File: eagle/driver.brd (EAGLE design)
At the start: 101.6 x 76.2 mm, 100 parts, among them IC1 XMEGA128A1, IC10 ST95P08M, IC11 ST95P08M, IC12 ST95P08M, IC13 ST95P08M, IC14 ST95P08M, IC15 ST95P08M, IC16 74AHC1G02DBV, IC17 74AHC1G02DBV, IC18 74AHC1G125DBV, IC19 74AHC1G125DBV, IC2 74AC16244, IC20 ST95P08M, IC21 ST95P08M, IC22 ST95P08M, IC23 ST95P08M, IC24 ST95P08M, IC25 ST95P08M, IC3 74AC16244, IC4 74AC16244, IC5 74AC16244, IC6 74AC16374, IC7 74AC16374, IC8 74AC16374, IC9 74AC16374, SW1 FSM2JSMA

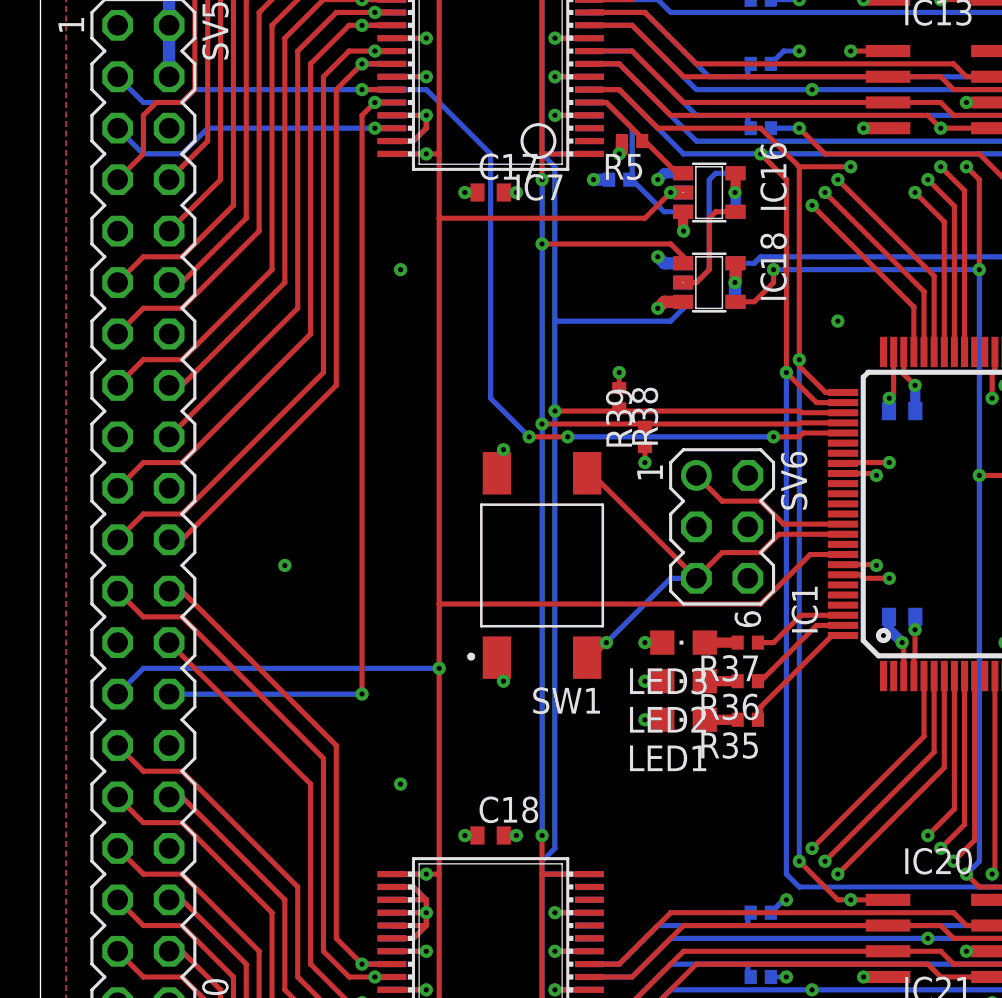
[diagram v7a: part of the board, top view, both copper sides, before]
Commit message: additional pull-up resistors
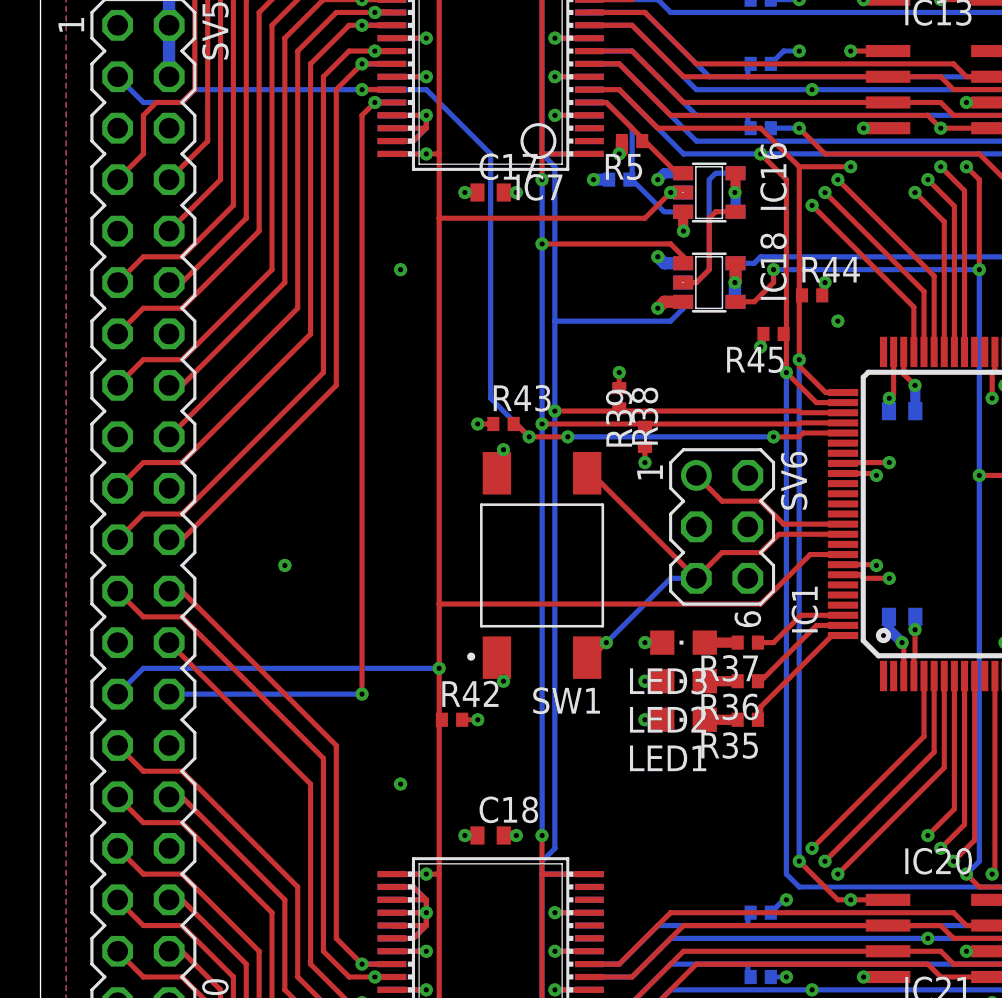
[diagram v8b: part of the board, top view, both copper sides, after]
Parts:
- added R42, R43, R44, R45: 33k, rcl:R0402
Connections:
- removed net N$92: IC6.27, IC7.46, SV5.5
- removed net N$99: IC1.92, IC16.2, IC17.2, IC6.25, IC6.48, IC7.25, IC7.48, IC8.25, IC8.48, IC9.25, IC9.48, SV5.27
- new net CLKIN: IC1.92, IC16.2, IC17.2, IC6.25, IC6.48, IC7.25, IC7.48, IC8.25, IC8.48, IC9.25, IC9.48, R42.1, SV5.27
- net GND: now also IC6.27, IC7.46, R42.2
- net VCC: now also R43.1, R44.2, R45.2
- net VSYNC: now also R43.2
- net VSYNC0: now also R45.1
- net VSYNC1: now also R44.1
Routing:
- net CLKIN: track 0.00 -> 130.9 mm, vias 0 -> 6
- net N$99: track 130.7 -> 0.00 mm, vias 6 -> 0
- net N$92: track 15.4 -> 0.00 mm, vias 1 -> 0
- net GND: track 194.6 -> 198.8 mm, vias 102 -> 103
- net VCC: track 86.1 -> 88.3 mm, vias 36 -> 39
- net VSYNC: track 52.3 -> 53.4 mm
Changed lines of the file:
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@@
 <attribute name="VALUE" x="70.485" y="39.37" size="1.27" layer="27" rot="R270"/>
+</element>
+<element name="R42" library="rcl" library_urn="urn:adsk.eagle:library:334" package="R0402" package3d_urn="urn:adsk.eagle:package:23547/3" value="33k" x="20.32" y="27.94" smashed="yes">
+<attribute name="NAME" x="19.685" y="28.575" size="1.27" layer="25"/>
+<attribute name="POPULARITY" value="34" x="20.32" y="27.94" size="1.778" layer="27" display="off"/>
+<attribute name="SPICEPREFIX" value="R" x="20.32" y="27.94" size="1.778" layer="27" display="off"/>
+<attribute name="VALUE" x="19.685" y="26.035" size="1.27" layer="27"/>
+</element>
+<element name="R43" library="rcl" library_urn="urn:adsk.eagle:library:334" package="R0402" package3d_urn="urn:adsk.eagle:package:23547/3" value="33k" x="22.86" y="42.545" smashed="yes">
+<attribute name="NAME" x="22.225" y="43.18" size="1.27" layer="25"/>
+<attribute name="POPULARITY" value="34" x="22.86" y="42.545" size="1.778" layer="27" display="off"/>
+<attribute name="SPICEPREFIX" value="R" x="22.86" y="42.545" size="1.778" layer="27" display="off"/>
+<attribute name="VALUE" x="22.225" y="40.64" size="1.27" layer="27"/>
+</element>
+<element name="R44" library="rcl" library_urn="urn:adsk.eagle:library:334" package="R0402" package3d_urn="urn:adsk.eagle:package:23547/3" value="33k" x="38.1" y="48.895" smashed="yes">
+<attribute name="NAME" x="37.465" y="49.53" size="1.27" layer="25"/>
+<attribute name="POPULARITY" value="34" x="38.1" y="48.895" size="1.778" layer="27" display="off"/>
+<attribute name="SPICEPREFIX" value="R" x="38.1" y="48.895" size="1.778" layer="27" display="off"/>
+<attribute name="VALUE" x="37.465" y="46.99" size="1.27" layer="27"/>
+</element>
+<element name="R45" library="rcl" library_urn="urn:adsk.eagle:library:334" package="R0402" package3d_urn="urn:adsk.eagle:package:23547/3" value="33k" x="36.195" y="46.99" smashed="yes" rot="R180">
+<attribute name="NAME" x="36.83" y="46.355" size="1.27" layer="25" rot="R180"/>
+<attribute name="POPULARITY" value="34" x="36.195" y="46.99" size="1.778" layer="27" rot="R180" display="off"/>
+<attribute name="SPICEPREFIX" value="R" x="36.195" y="46.99" size="1.778" layer="27" rot="R180" display="off"/>
+<attribute name="VALUE" x="36.83" y="48.895" size="1.27" layer="27" rot="R180"/>
 </element>
 </elements>
@@
 <wire x1="17.3482" y1="17.145" x2="18.415" y2="17.145" width="0.254" layer="1"/>
 <wire x1="18.415" y1="17.145" x2="19.05" y2="17.78" width="0.254" layer="1"/>
+<contactref element="IC6" pad="27"/>
+<contactref element="IC7" pad="46"/>
+<wire x1="17.3482" y1="57.15" x2="19.05" y2="57.15" width="0.254" layer="16"/>
+<wire x1="17.3482" y1="57.15" x2="19.05" y2="57.15" width="0.254" layer="1"/>
+<contactref element="R42" pad="2"/>
+<via x="21.59" y="27.94" extent="1-16" drill="0.254"/>
+<wire x1="20.82" y1="27.94" x2="21.59" y2="27.94" width="0.254" layer="1"/>
 </signal>
 <signal name="VCC">
@@
 <wire x1="72.39" y1="38.235" x2="72.39" y2="37.465" width="0.254" layer="1"/>
 <wire x1="71.12" y1="41.14" x2="71.12" y2="41.91" width="0.254" layer="1"/>
+<contactref element="R43" pad="1"/>
+<via x="21.59" y="42.545" extent="1-16" drill="0.254"/>
+<wire x1="22.36" y1="42.545" x2="21.59" y2="42.545" width="0.254" layer="1"/>
+<contactref element="R45" pad="2"/>
+<contactref element="R44" pad="2"/>
+<via x="38.735" y="49.53" extent="1-16" drill="0.254"/>
+<via x="35.56" y="46.355" extent="1-16" drill="0.254"/>
+<wire x1="38.6" y1="48.895" x2="38.6" y2="49.395" width="0.254" layer="1"/>
+<wire x1="38.6" y1="49.395" x2="38.735" y2="49.53" width="0.254" layer="1"/>
+<wire x1="35.695" y1="46.99" x2="35.695" y2="46.49" width="0.254" layer="1"/>
+<wire x1="35.695" y1="46.49" x2="35.56" y2="46.355" width="0.254" layer="1"/>
 </signal>
 <signal name="N$1">
@@
 <wire x1="34.925" y1="18.28" x2="34.925" y2="17.78" width="0.254" layer="16"/>
 </signal>
-<signal name="N$92">
-<contactref element="IC6" pad="27"/>
-<contactref element="IC7" pad="46"/>
-<contactref element="SV5" pad="5"/>
-<wire x1="16.51" y1="57.15" x2="17.3482" y2="57.15" width="0.254" layer="16"/>
-<via x="16.51" y="57.15" extent="1-16" drill="0.254"/>
-<wire x1="17.3482" y1="57.15" x2="16.51" y2="57.15" width="0.254" layer="1"/>
-<wire x1="3.81" y1="57.15" x2="5.08" y2="55.88" width="0.254" layer="16"/>
-<wire x1="5.08" y1="55.88" x2="6.985" y2="55.88" width="0.254" layer="16"/>
-<wire x1="6.985" y1="55.88" x2="8.255" y2="57.15" width="0.254" layer="16"/>
-<wire x1="8.255" y1="57.15" x2="16.51" y2="57.15" width="0.254" layer="16"/>
-</signal>
 <signal name="N$93">
 <contactref element="IC7" pad="44"/>
@@
 <wire x1="39.625" y1="43.6" x2="38.315" y2="43.6" width="0.254" layer="1"/>
 <wire x1="38.315" y1="43.6" x2="36.83" y2="45.085" width="0.254" layer="1"/>
-<wire x1="36.83" y1="45.085" x2="36.83" y2="54.61" width="0.254" layer="1"/>
+<wire x1="36.83" y1="45.085" x2="36.83" y2="46.99" width="0.254" layer="1"/>
+<wire x1="36.83" y1="46.99" x2="36.83" y2="54.61" width="0.254" layer="1"/>
 <wire x1="36.83" y1="54.61" x2="35.56" y2="55.88" width="0.254" layer="1"/>
 <via x="35.56" y="55.88" extent="1-16" drill="0.254"/>
@@
 <wire x1="37.465" y1="19.685" x2="36.83" y2="20.32" width="0.254" layer="16"/>
 <wire x1="36.83" y1="20.32" x2="36.83" y2="45.085" width="0.254" layer="16"/>
+<contactref element="R45" pad="1"/>
+<wire x1="36.695" y1="46.99" x2="36.83" y2="46.99" width="0.254" layer="1"/>
 </signal>
 <signal name="VSYNC1">
@@
 <contactref element="IC1" pad="76"/>
 <wire x1="37.465" y1="45.4025" x2="37.465" y2="45.72" width="0.254" layer="1"/>
-<wire x1="37.465" y1="45.72" x2="37.465" y2="55.245" width="0.254" layer="1"/>
+<wire x1="37.465" y1="45.72" x2="37.465" y2="48.895" width="0.254" layer="1"/>
+<wire x1="37.465" y1="48.895" x2="37.465" y2="55.245" width="0.254" layer="1"/>
 <wire x1="39.625" y1="44.1" x2="38.7675" y2="44.1" width="0.254" layer="1"/>
 <wire x1="38.7675" y1="44.1" x2="37.465" y2="45.4025" width="0.254" layer="1"/>
@@
 <wire x1="37.465" y1="45.72" x2="37.465" y2="20.955" width="0.254" layer="16"/>
 <via x="37.465" y="20.955" extent="1-16" drill="0.254"/>
+<contactref element="R44" pad="1"/>
+<wire x1="37.6" y1="48.895" x2="37.465" y2="48.895" width="0.254" layer="1"/>
 </signal>
 <signal name="N$110">
@@
 <wire x1="36.195" y1="50.165" x2="46.355" y2="50.165" width="0.254" layer="16"/>
 </signal>
-<signal name="N$99">
+<signal name="CLKIN">
 <contactref element="IC17" pad="2"/>
 <contactref element="IC6" pad="48"/>
@@
 <wire x1="19.685" y1="33.655" x2="19.685" y2="52.705" width="0.254" layer="1"/>
 <wire x1="19.685" y1="52.705" x2="19.685" y2="55.88" width="0.254" layer="1"/>
-<wire x1="19.685" y1="30.48" x2="19.685" y2="20.32" width="0.254" layer="1"/>
+<wire x1="19.685" y1="30.48" x2="19.685" y2="27.94" width="0.254" layer="1"/>
+<wire x1="19.685" y1="27.94" x2="19.685" y2="20.32" width="0.254" layer="1"/>
 <wire x1="19.685" y1="20.32" x2="19.685" y2="6.35" width="0.254" layer="1"/>
 <wire x1="19.685" y1="6.35" x2="19.05" y2="5.715" width="0.254" layer="1"/>
@@
 <wire x1="29.845" y1="52.705" x2="31.115" y2="53.975" width="0.254" layer="1"/>
 <wire x1="19.685" y1="52.705" x2="29.845" y2="52.705" width="0.254" layer="1"/>
+<contactref element="R42" pad="1"/>
+<wire x1="19.82" y1="27.94" x2="19.685" y2="27.94" width="0.254" layer="1"/>
 </signal>
 <signal name="N$30">
@@
 <via x="36.195" y="41.91" extent="1-16" drill="0.254"/>
 <wire x1="26.035" y1="41.91" x2="36.195" y2="41.91" width="0.254" layer="16"/>
+<contactref element="R43" pad="2"/>
+<wire x1="23.36" y1="42.545" x2="23.495" y2="42.545" width="0.254" layer="1"/>
+<wire x1="23.495" y1="42.545" x2="24.13" y2="41.91" width="0.254" layer="1"/>
 </signal>
 <signal name="N$87">
